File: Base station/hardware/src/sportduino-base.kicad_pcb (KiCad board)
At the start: 2 copper layers, 54.6 x 26.7 mm, 23 parts, among them X1 Battery, X2 RC522, X3 Pickit2, X4 Bootloader

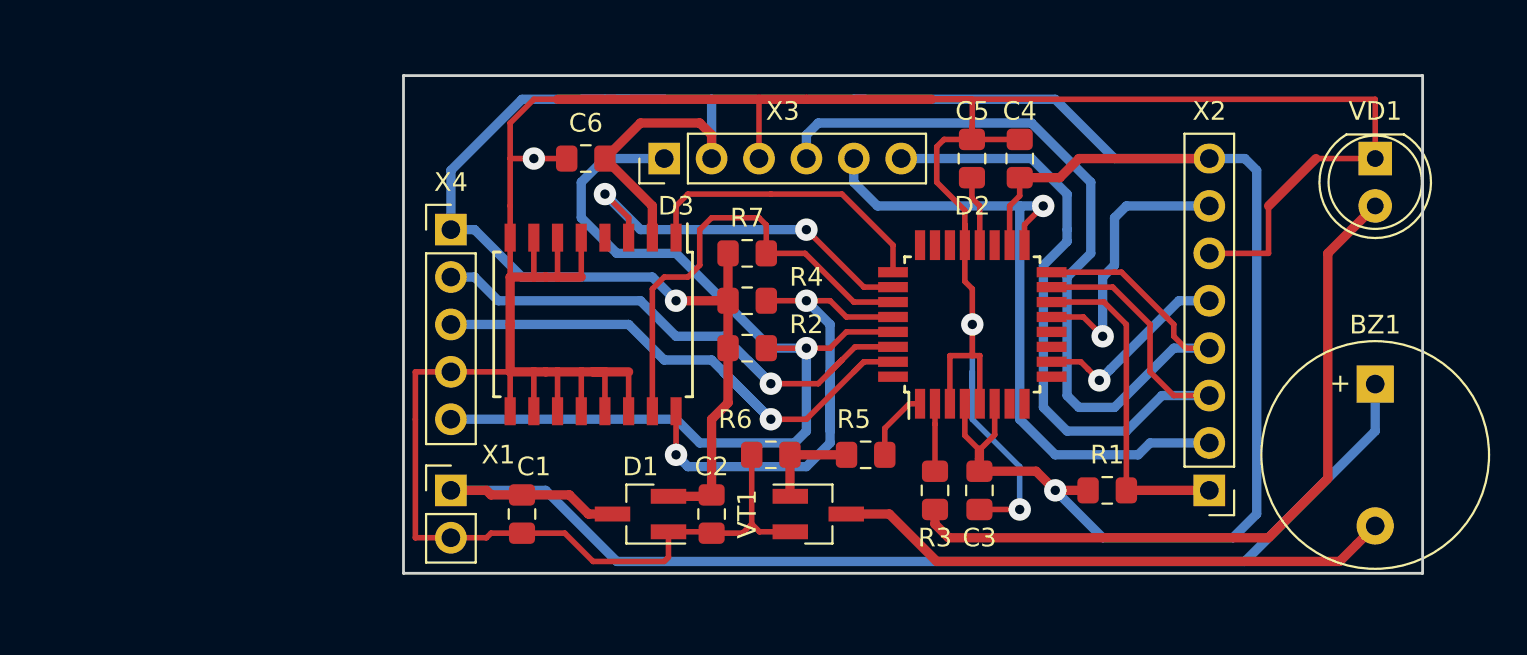
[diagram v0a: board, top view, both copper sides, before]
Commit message: Немного улучшил трассировку ПП: добавил переходных отверстий GND для увеличения области металлизации
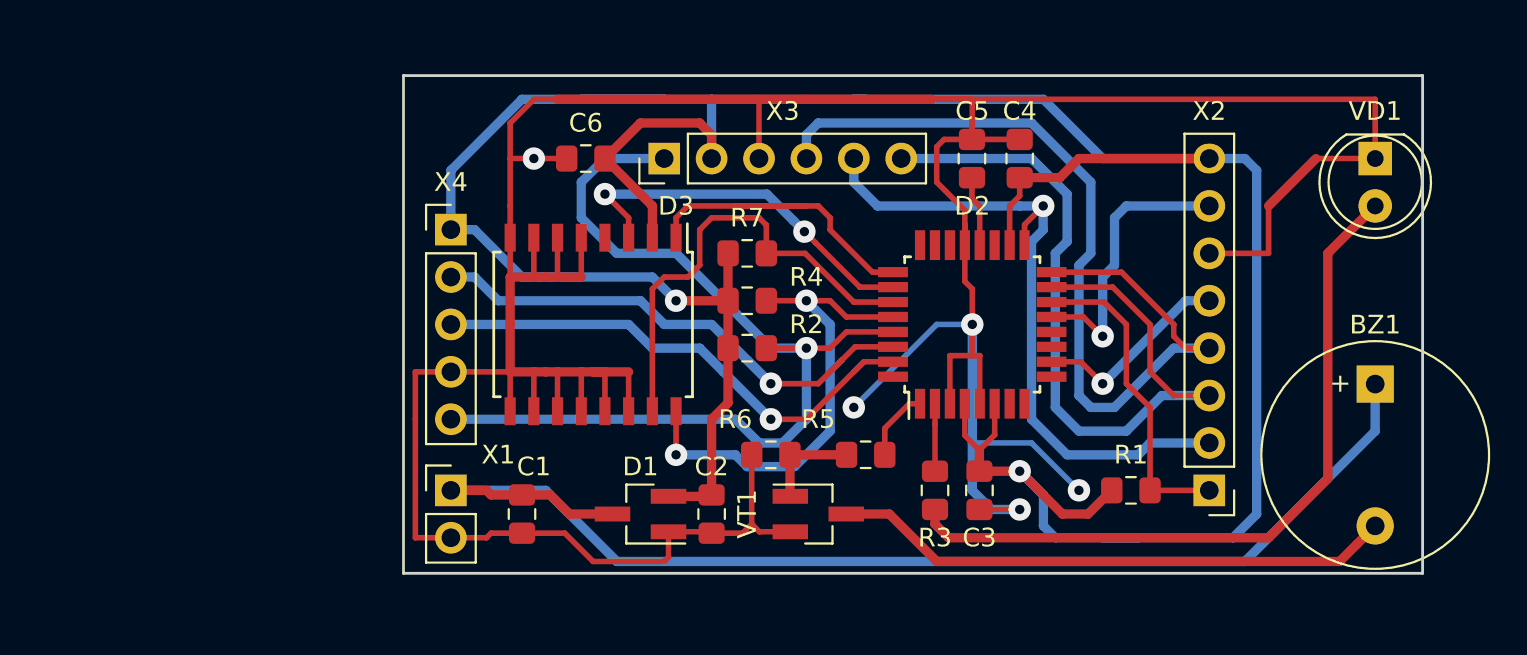
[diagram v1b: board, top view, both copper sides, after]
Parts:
- moved R1 1.27 mm to (183.8, 100.3)
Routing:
- net GNDD: track 196.4 -> 211.0 mm, vias 3 -> 5
- net +3V3: track 162.0 -> 169.6 mm
- net TX: track 31.4 -> 27.8 mm
- net Net-(D2-Pad28): track 29.9 -> 26.3 mm
- net RX: track 32.3 -> 29.6 mm
- net PC2: track 16.2 -> 18.6 mm
- net /PB3: track 44.2 -> 43.3 mm
- net /PB4: track 50.3 -> 49.4 mm
- net /PB2: track 17.8 -> 17.1 mm

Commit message: Исправил собственную ошибку в схеме: 32кГц надо подключать на счетный вход МК
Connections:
- D2 pad 25: PC2 -> (no net)
- D2 pad 9: (no net) -> PD5
- D3 pad 1: PC2 -> PD5
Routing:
- net PD5: track 0.00 -> 42.6 mm, vias 0 -> 2
- net PC2: track 18.6 -> 0.00 mm
- net /PB2: track 17.1 -> 18.8 mm
- net /PB5: track 36.7 -> 35.1 mm
- net /PB3: track 43.3 -> 44.8 mm
- net /PB4: track 49.4 -> 50.5 mm
- net /PB1: track 15.1 -> 14.0 mm
- net PD6: track 10.8 -> 9.80 mm

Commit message: 1. В схеме подключил выход RST микросхемы DS3231 к MCU 2. Для выхода 32 кГц добавил внешний подтягивающий резистор, потому что с внутренним сильно срезаются фронты
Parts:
- removed the R1 at (183.8, 100.3)
- added R7: 3K3, Resistor_SMD:R_0805_2012Metric_Pad1.15x1.40mm_HandSolder, F.Cu at (184.2, 99.5)
- R4: renamed from R5; value 3K6 -> 3K3
- moved R5 3.24 mm to (163.8, 101.6), turned to 90 degrees
- moved VT1 0.63 mm to (167.6, 101.6)
- moved R4 0.25 mm to (169.8, 98.4)
- renumbered R2 to R1, R3 to R2, R4 to R3, R6 to R5, R7 to R6
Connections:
- net Net-(D2-Pad27) renamed /SDA
- net Net-(D2-Pad28) renamed /SCL
- D2 pad 32: (no net) -> Net-(D2-Pad32)
- D3 pad 4: (no net) -> Net-(D2-Pad32)
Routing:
- net Net-(D2-Pad32): track 0.00 -> 24.9 mm, vias 0 -> 2
- net GNDD: track 211.0 -> 195.6 mm, vias 5 -> 4
- net +3V3: track 169.6 -> 167.5 mm
- net TX: track 27.8 -> 29.3 mm
- net /SCL: track 26.3 -> 27.6 mm
- net /PB2: track 18.8 -> 17.7 mm
- net Net-(R4-Pad1): track 5.26 -> 6.30 mm
- net PD5: track 42.6 -> 43.6 mm
- net Net-(BZ1-Pad2): track 30.2 -> 29.6 mm
- net +BATT: track 65.7 -> 66.3 mm, vias 0 -> 1

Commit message: 1. Изменил разъём X4 для подключения преобразователя USB-to-TTL под китайский на FT232RL 2. Поправил диаметры отверстий и размеры контактных площадок
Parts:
- added BZ1*: PinHeader_1x01_P2.54mm_Vertical, Connector_PinHeader_2.54mm:PinHeader_1x01_P2.54mm_Vertical, F.Cu at (196.8, 98.2)
- VD1: value 5mm -> 3mm; footprint LED_THT:LED_D5.0mm -> LED_THT:LED_D3.0mm
- X4: value Bootloader -> Serial; footprint Connector_PinHeader_2.54mm:PinHeader_1x05_P2.54mm_Vertical -> Connector_PinSocket_2.54mm:PinSocket_1x06_P2.54mm_Vertical
- moved X4 8.89 mm to (147.3, 95.2), turned to 180 degrees
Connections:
- X4 pad 1: +3V3 -> RST
- X4 pad 2: RX -> TX
- X4 pad 3: TX -> RX
- X4 pad 4: GNDD -> (no net)
- X4 pad 5: RST -> (no net)
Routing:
- net +3V3: track 167.5 -> 149.7 mm
- net GNDD: track 195.6 -> 208.3 mm
- net RST: track 52.9 -> 54.3 mm
- net TX: track 29.3 -> 29.8 mm
- net RX: track 29.6 -> 29.0 mm
- net +BATT: vias 1 -> 0

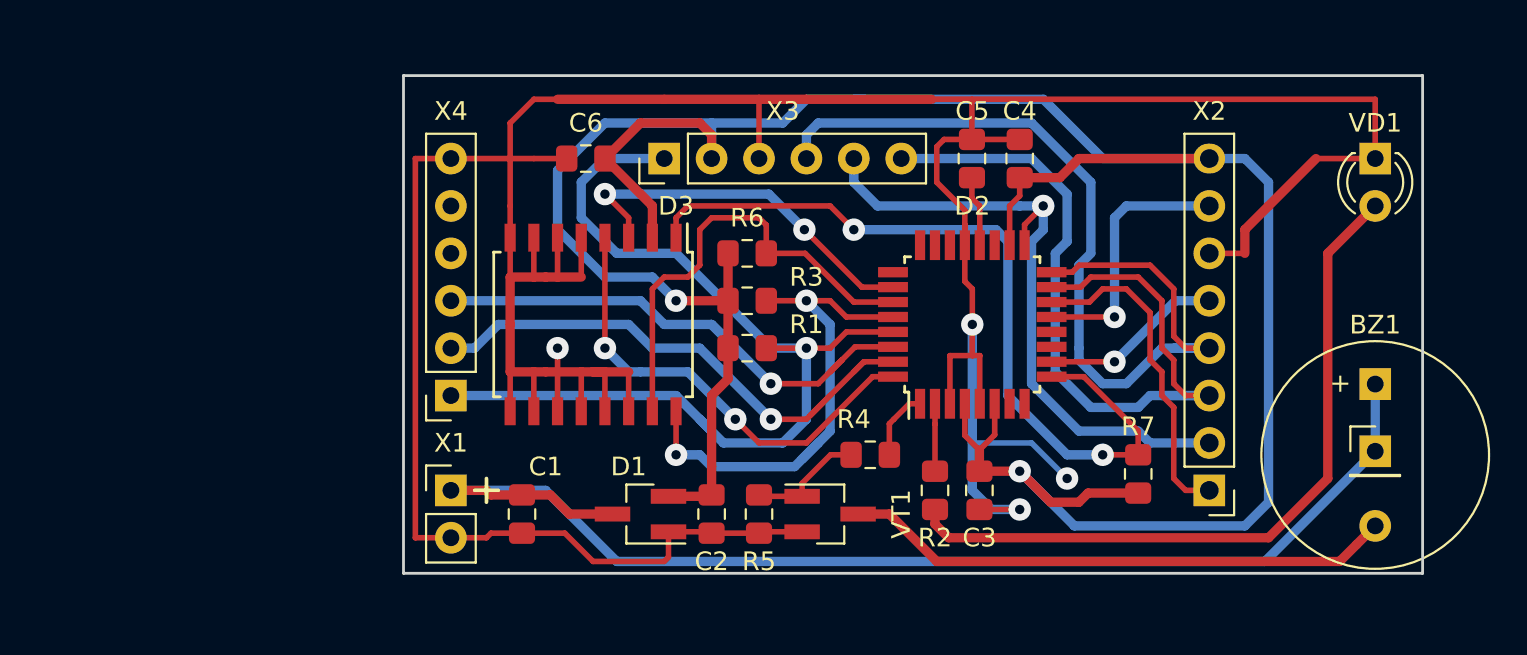
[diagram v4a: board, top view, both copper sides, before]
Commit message: Схема и плата версия 3: 1. Исправил подключение питания для DS3231 2. UART и SPI для программирования вынес на один разъём 3. Добавил цепь для измерения напряжения на батарее 4. Добавил тестовых точек 5. Добавил конденсатор на цепь DTR 6. Добавил фильтр на цепь RST
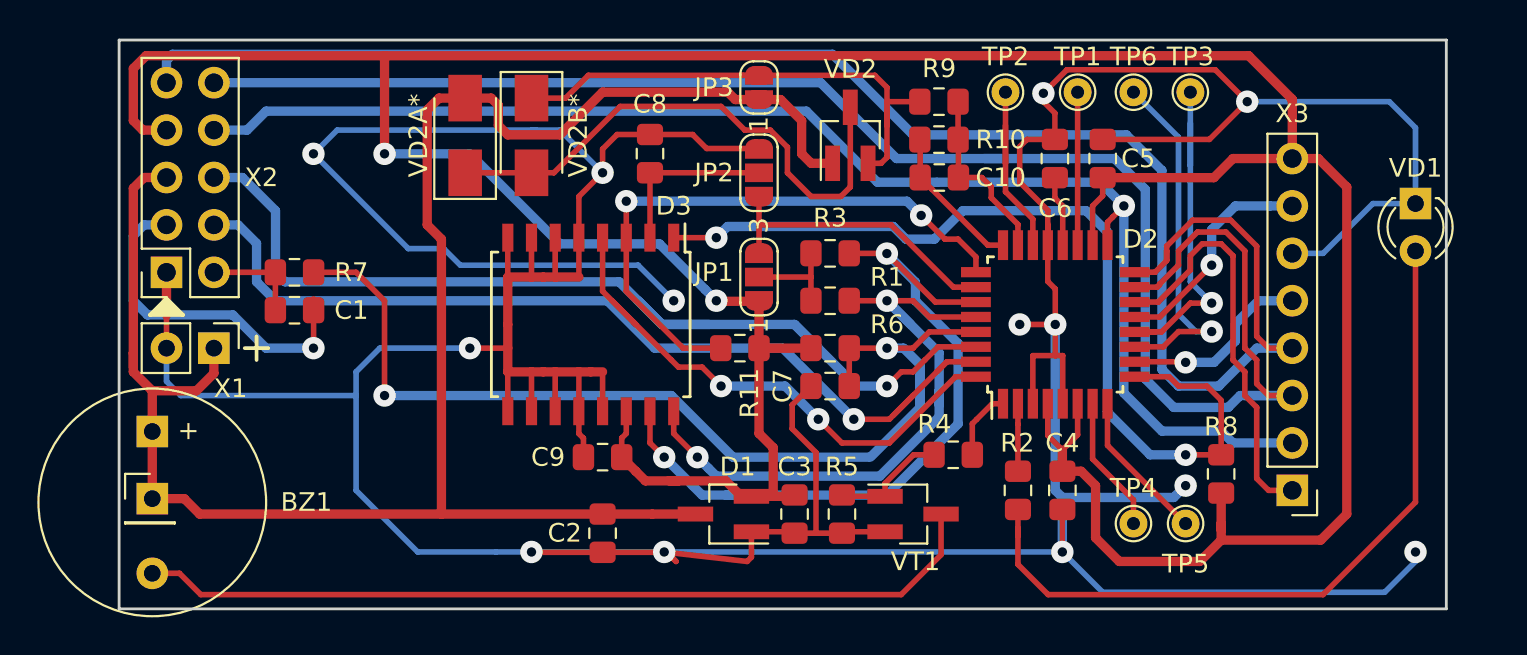
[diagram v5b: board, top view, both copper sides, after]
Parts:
- removed X4: Serial, Connector_PinSocket_2.54mm:PinSocket_1x06_P2.54mm_Vertical
- added C10: 100 nF, Capacitor_SMD:C_0805_2012Metric_Pad1.15x1.40mm_HandSolder, F.Cu at (173.5, 83.6)
- added C7: 100 nF, Capacitor_SMD:C_0805_2012Metric_Pad1.15x1.40mm_HandSolder, F.Cu at (167.6, 94.7)
- added C8: 100 nF, Capacitor_SMD:C_0805_2012Metric_Pad1.15x1.40mm_HandSolder, F.Cu at (158.0, 82.3)
- added C9: 100 nF, Capacitor_SMD:C_0805_2012Metric_Pad1.15x1.40mm_HandSolder, F.Cu at (155.4, 98.6)
- added JP1: SolderJumper_3_Bridged12, Jumper:SolderJumper-3_P1.3mm_Open_RoundedPad1.0x1.5mm_NumberLabels, F.Cu at (163.8, 88.9)
- added JP2: SolderJumper_3_Bridged12, Jumper:SolderJumper-3_P1.3mm_Open_RoundedPad1.0x1.5mm_NumberLabels, F.Cu at (163.8, 83.3)
- added JP3: SolderJumper_2_Open, Jumper:SolderJumper-2_P1.3mm_Open_RoundedPad1.0x1.5mm, F.Cu at (163.8, 78.7)
- added R10: 30K, Resistor_SMD:R_0805_2012Metric_Pad1.15x1.40mm_HandSolder, F.Cu at (173.5, 81.5)
- added R11: 3K3, Resistor_SMD:R_0805_2012Metric_Pad1.15x1.40mm_HandSolder, F.Cu at (162.8, 92.7)
- added R8: 3K3, Resistor_SMD:R_0805_2012Metric_Pad1.15x1.40mm_HandSolder, F.Cu at (188.6, 99.5)
- added R9: 100K, Resistor_SMD:R_0805_2012Metric_Pad1.15x1.40mm_HandSolder, F.Cu at (173.5, 79.5)
- added TP1: TestPoint, TestPoint:TestPoint_THTPad_D1.5mm_Drill0.7mm, F.Cu at (180.9, 79.0)
- added TP2: TestPoint, TestPoint:TestPoint_THTPad_D1.5mm_Drill0.7mm, F.Cu at (177.0, 79.0)
- added TP3: TestPoint, TestPoint:TestPoint_THTPad_D1.5mm_Drill0.7mm, F.Cu at (186.9, 79.0)
- added TP4: TestPoint, TestPoint:TestPoint_THTPad_D1.5mm_Drill0.7mm, F.Cu at (183.9, 102.1)
- added TP5: TestPoint, TestPoint:TestPoint_THTPad_D1.5mm_Drill0.7mm, F.Cu at (186.7, 102.1)
- added TP6: TestPoint, TestPoint:TestPoint_THTPad_D1.5mm_Drill0.7mm, F.Cu at (183.9, 79.0)
- added VD2: BAV99, Package_TO_SOT_SMD:SOT-23_Handsoldering, F.Cu at (168.7, 81.3)
- added VD2A*: D_SMA, Diode_SMD:D_SMA, F.Cu at (148.1, 81.3)
- added VD2B*: D_SMA, Diode_SMD:D_SMA, F.Cu at (151.6, 81.3)
- C1: value 1 uF -> 100 nF
- C2: value 1 uF -> 4.7 uF
- C3: value 100 nF -> 4.7 uF
- R1: value 33K -> 10K
- R3: value 3K3 -> 10K
- R6: value 3K3 -> 33K
- R7: value 3K3 -> 100
- X2: value RC522 -> Prog; footprint Connector_PinHeader_2.54mm:PinHeader_1x08_P2.54mm_Vertical -> Connector_PinSocket_2.54mm:PinSocket_2x05_P2.54mm_Vertical
- X3: value Pickit2 -> RC522; footprint Connector_PinHeader_2.54mm:PinHeader_1x06_P2.54mm_Vertical -> Connector_PinHeader_2.54mm:PinHeader_1x08_P2.54mm_Vertical
- moved BZ1* 65.7 mm to (131.2, 100.8)
- moved BZ1 65.6 mm to (131.3, 97.2)
- moved X2 57.1 mm to (132.1, 88.6)
- moved R7 46.5 mm to (138.9, 88.6), turned to 180 degrees
- moved X3 38.1 mm to (192.4, 100.3), turned to 180 degrees
- moved C6 25.1 mm to (179.7, 82.5), turned to 90 degrees
- moved C4 17.9 mm to (180.1, 100.3), turned to 270 degrees
- moved C1 16.4 mm to (138.9, 90.7), turned to 0 degrees
- moved X1 14.8 mm to (134.6, 92.7), turned to 270 degrees
- moved C3 9.99 mm to (165.7, 101.6)
- moved C5 7.00 mm to (182.2, 82.5)
- moved R6 6.75 mm to (167.6, 92.7)
- moved C2 5.93 mm to (155.4, 102.6)
- moved R3 5.12 mm to (167.6, 87.6)
- moved R1 5.12 mm to (167.6, 90.2)
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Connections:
- net Net-(D2-Pad1) renamed /BUZ
- net Net-(D2-Pad2) renamed /LED
- BZ1* pad 1: (no net) -> +BATT
- C1 pad 1: +BATT -> RST
- C1 pad 2: GNDD -> Net-(C1-Pad2)
- C2 pad 1: +3V3 -> +BATT
- C5 pad 1: Net-(C5-Pad1) -> +3V3
- C6 pad 1: +3V3 -> Net-(C6-Pad1)
- D2 pad 11: (no net) -> Net-(D2-Pad11)
- D2 pad 12: (no net) -> Net-(D2-Pad12)
- D2 pad 15: /PB3 -> PB3
- D2 pad 16: /PB4 -> PB4
- D2 pad 17: /PB5 -> PB5
- D2 pad 19: (no net) -> Net-(D2-Pad19)
- D2 pad 20: Net-(C5-Pad1) -> Net-(C6-Pad1)
- D2 pad 22: (no net) -> Net-(D2-Pad22)
- D2 pad 23: (no net) -> ADCIN
- D2 pad 24: (no net) -> ADCEN
- D2 pad 25: (no net) -> ALARM
- D2 pad 26: PC3 -> /VCCR
- D2 pad 29: RST -> Net-(C7-Pad1)
- D2 pad 7: (no net) -> Net-(D2-Pad7)
- D2 pad 8: (no net) -> Net-(D2-Pad8)
- D2 pad 9: PD5 -> 32K
- D3 pad 1: PD5 -> 32K
- D3 pad 14: GNDD -> +3V3
- D3 pad 2: +3V3 -> Net-(C8-Pad1)
- D3 pad 3: PC3 -> ALARM
- R1 pad 1: +3V3 -> Net-(JP1-Pad2)
- R1 pad 2: RST -> /SCL
- R3 pad 1: +3V3 -> Net-(JP1-Pad2)
- R3 pad 2: /SCL -> /SDA
- R6 pad 2: /SDA -> Net-(C7-Pad1)
- R7 pad 1: +3V3 -> Net-(C7-Pad1)
- R7 pad 2: PD5 -> RST
- X2 pad 1: /PB2 -> GNDD
- X2 pad 2: /PB5 -> RST
- X2 pad 3: /PB3 -> Net-(C1-Pad2)
- X2 pad 4: /PB4 -> TX
- X2 pad 5: PD6 -> +BATT
- X2 pad 6: GNDD -> RX
- X2 pad 7: /PB1 -> +3V3
- X2 pad 8: +3V3 -> PB5
- X3 pad 1: RST -> /PB2
- X3 pad 2: +3V3 -> PB5
- X3 pad 3: GNDD -> PB3
- X3 pad 4: /PB4 -> PB4
- X3 pad 5: /PB5 -> PD6
- X3 pad 6: /PB3 -> GNDD
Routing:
- net GNDD: track 208.3 -> 302.7 mm, vias 4 -> 13
- net PB4: track 0.00 -> 92.9 mm
- net PB3: track 0.00 -> 92.5 mm
- net PB5: track 0.00 -> 73.9 mm, vias 0 -> 1
- net Net-(C7-Pad1): track 0.00 -> 56.3 mm, vias 0 -> 2
- net /PB4: track 50.5 -> 0.00 mm
- net 32K: track 0.00 -> 49.7 mm, vias 0 -> 2
- net RST: track 54.3 -> 5.33 mm, vias 1 -> 0
- net /PB3: track 44.8 -> 0.00 mm
- net PD5: track 43.6 -> 0.00 mm, vias 2 -> 0
- net +3V3: track 149.7 -> 192.1 mm
- net +BATT: track 66.3 -> 103.3 mm
- net /PB5: track 35.1 -> 0.00 mm, vias 1 -> 0
- net ALARM: track 0.00 -> 32.5 mm, vias 0 -> 2
- net Net-(VD2-Pad3): track 0.00 -> 29.4 mm
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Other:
- board size 54.6 x 26.7 mm -> 71.1 x 30.5 mm
- net class power: via_dia 1.8 -> 1.2; via_drill 0.7 -> 0.5
- board text added: "G1020BF"
- board text added: "RC522"

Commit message: Убрал с печатной платы области металлизации, иначе они экранируют антенну
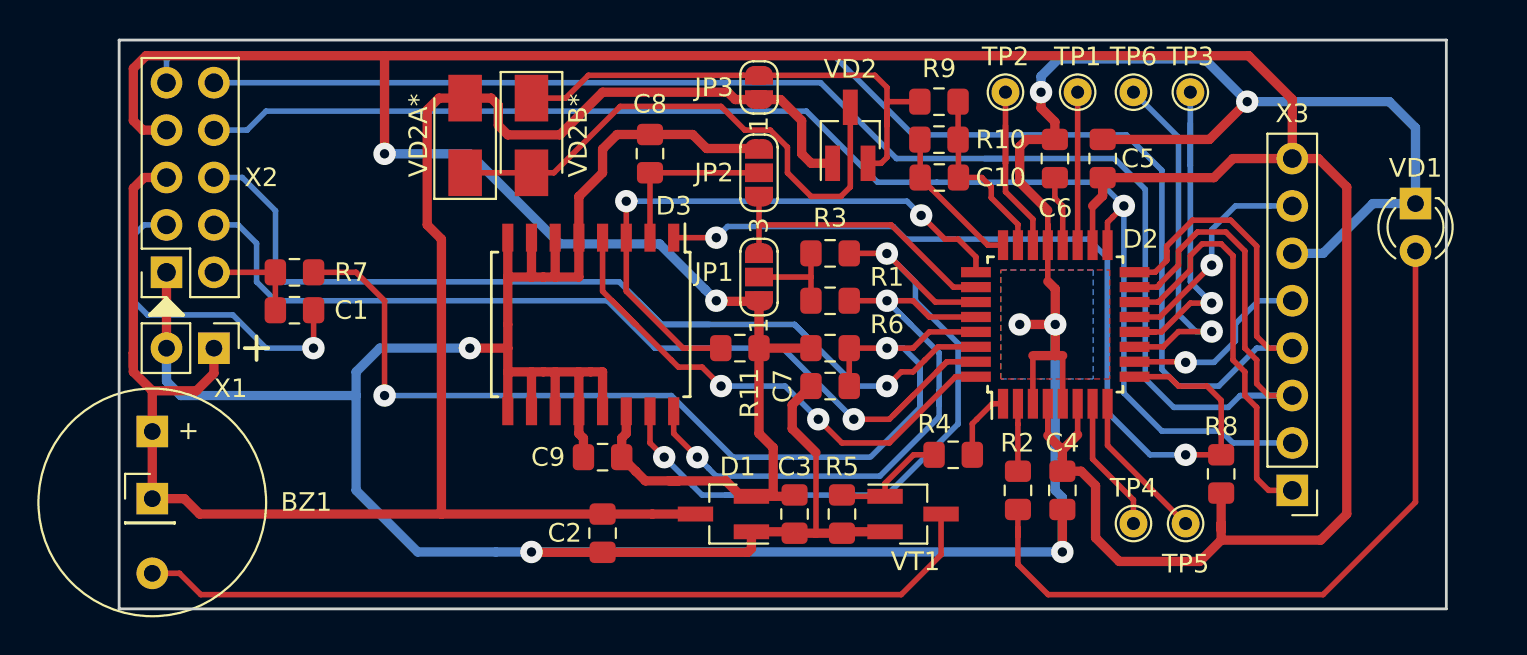
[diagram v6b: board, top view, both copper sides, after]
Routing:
- net GNDD: track 302.7 -> 234.4 mm, vias 13 -> 7
- net 32K: track 49.7 -> 47.6 mm
